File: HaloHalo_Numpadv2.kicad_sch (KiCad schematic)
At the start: 92 parts, among them SW1 SW_SPST, SW10 SW_SPST, SW11 SW_SPST, SW12 SW_SPST, SW13 SW_SPST, SW14 SW_SPST, SW15 SW_SPST, SW16 SW_SPST, SW17 SW_SPST, SW18 SW_SPST, SW19 SW_SPST, SW2 SW_SPST, SW20 SW_SPST, SW21 RotaryEncoder_Switch, SW22 RotaryEncoder_Switch, SW23 RotaryEncoder_Switch, SW3 SW_SPST, SW4 SW_SPST, SW5 SW_SPST, SW6 SW_SPST, SW7 SW_SPST, SW8 SW_SPST, SW9 SW_SPST

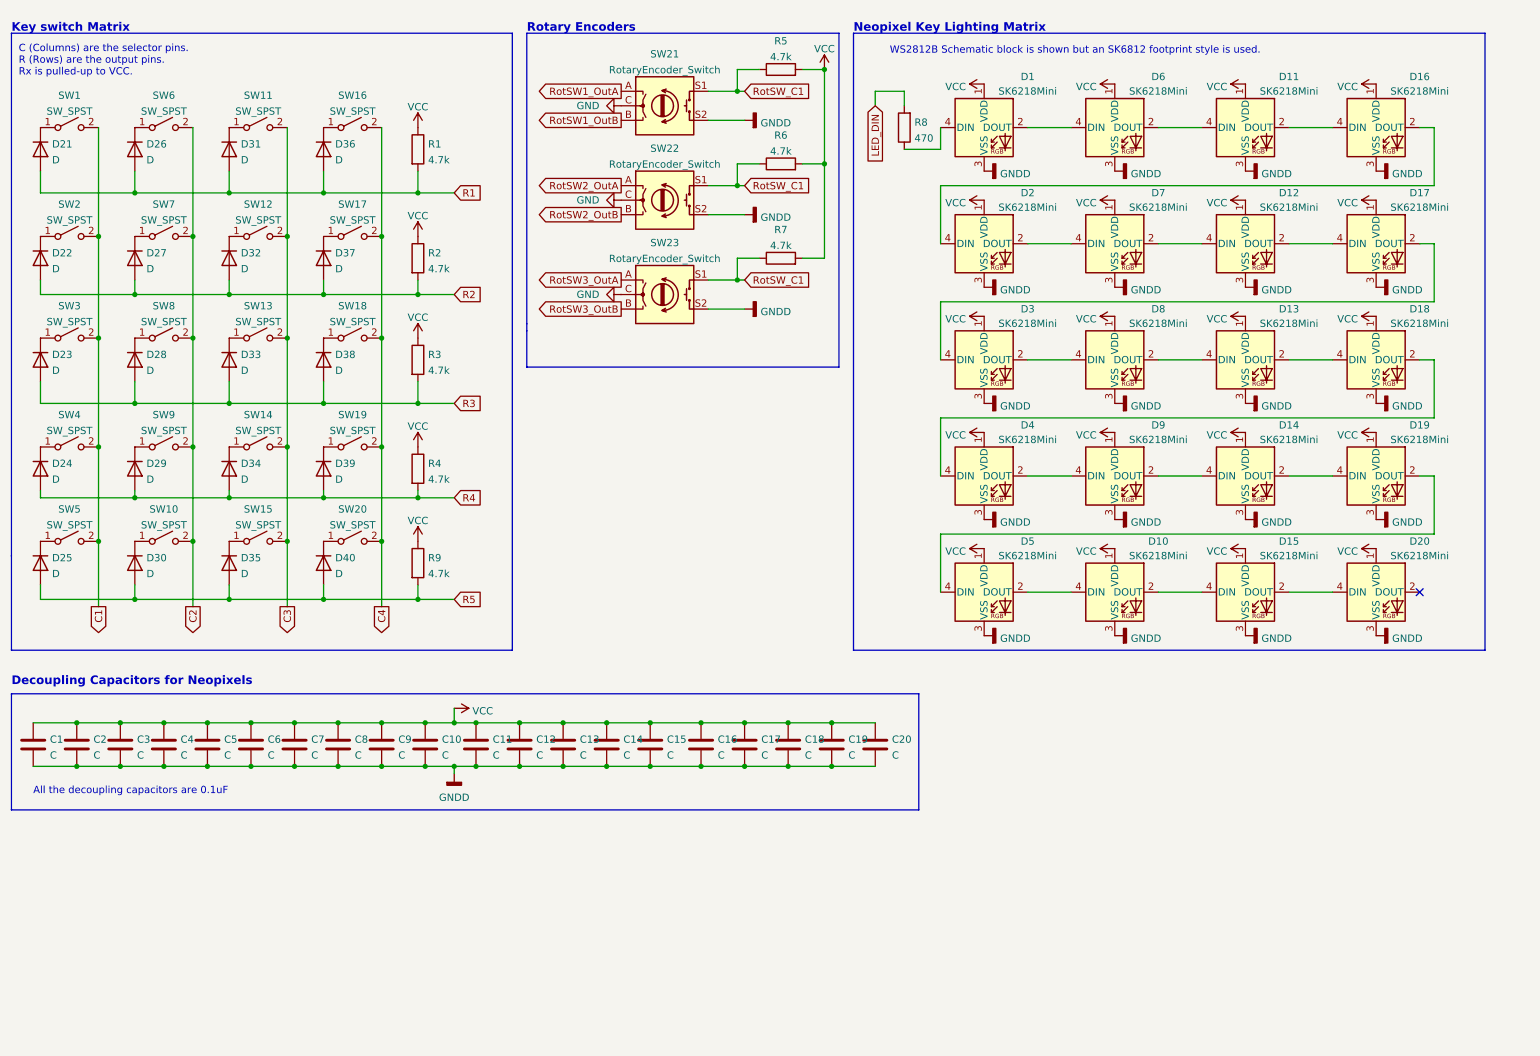
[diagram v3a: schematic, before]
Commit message: Updated Schematic and PCB to include headers for OLED display. Need to update corresponding PDFs and images.
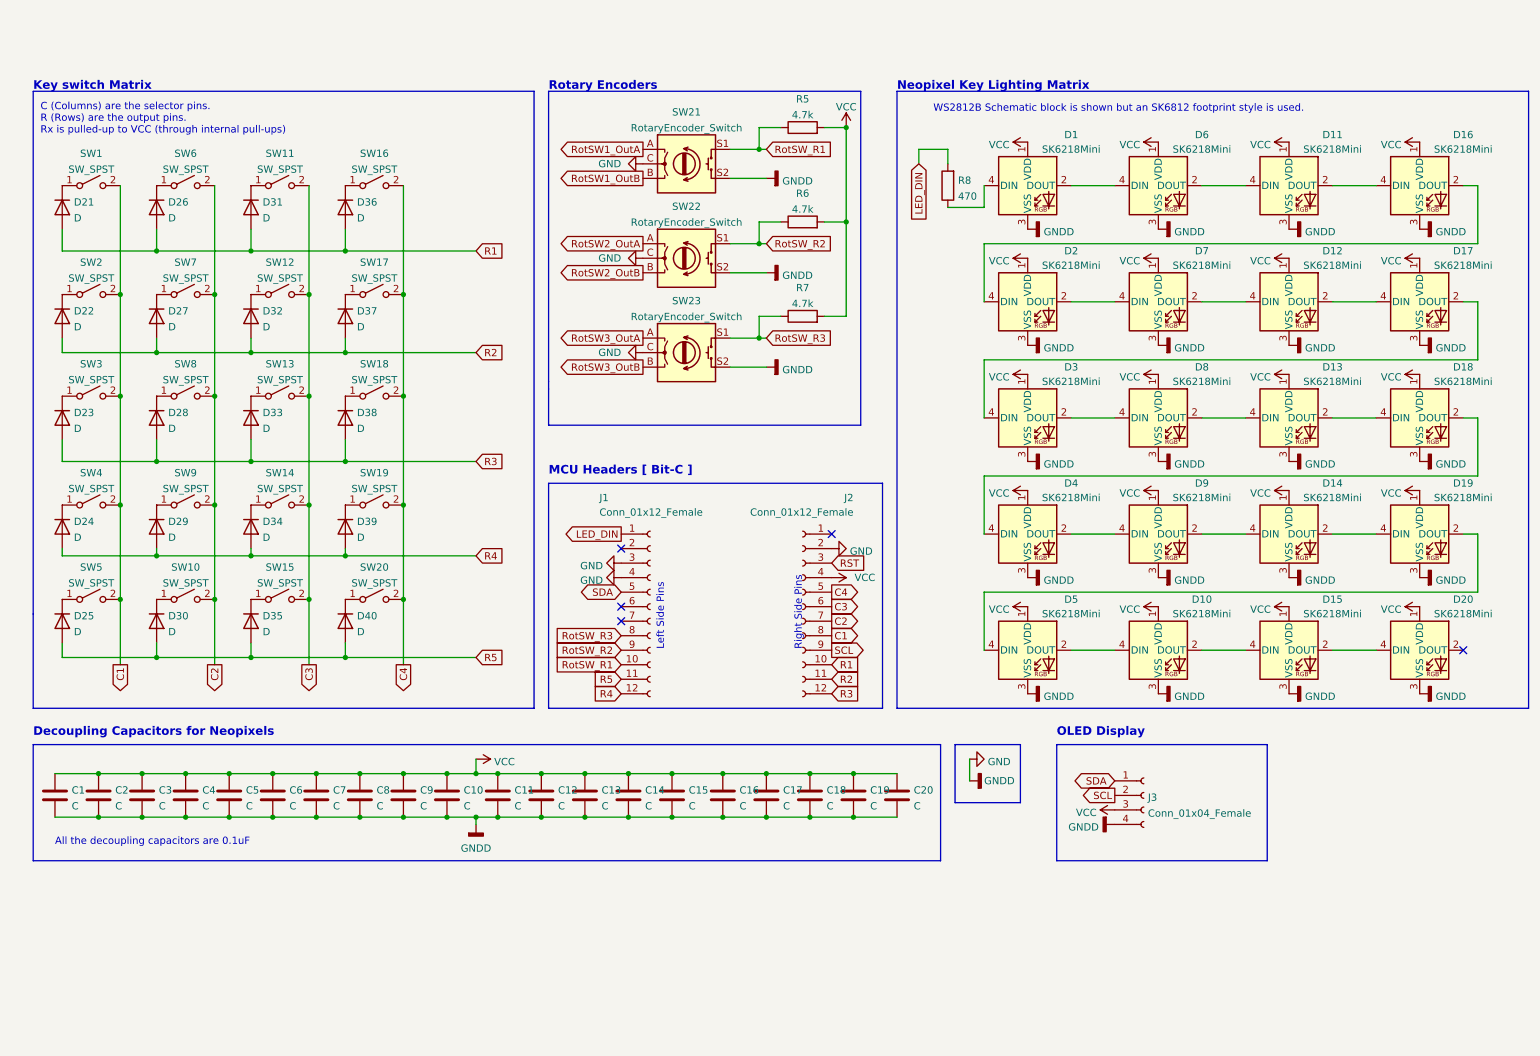
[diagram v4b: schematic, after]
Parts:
- removed R1, R2, R3, R4, R9: 4.7k, Resistor_THT:R_Axial_DIN0204_L3.6mm_D1.6mm_P5.08mm_Horizontal, symbol Device:R
- added J1, J2: Conn_01x12_Female, Connector_PinSocket_2.54mm:PinSocket_1x12_P2.54mm_Vertical, symbol Connector:Conn_01x12_Female
- added J3: Conn_01x04_Female, Connector_PinSocket_2.54mm:PinSocket_1x04_P2.54mm_Vertical, symbol Connector:Conn_01x04_Female
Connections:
- net GNDD is gone; now on net GND: C1.2, C10.2, C11.2, C12.2, C13.2, C14.2, C15.2, C16.2, C17.2, C18.2, C19.2, C2.2, C20.2, C3.2, C4.2, C5.2, C6.2, C7.2, C8.2, C9.2, D1.3 (VSS), D10.3 (VSS), D11.3 (VSS), D12.3 (VSS), D13.3 (VSS), D14.3 (VSS), D15.3 (VSS), D16.3 (VSS), D17.3 (VSS), D18.3 (VSS), D19.3 (VSS), D2.3 (VSS), D20.3 (VSS), D3.3 (VSS), D4.3 (VSS), D5.3 (VSS), D6.3 (VSS), D7.3 (VSS), D8.3 (VSS), D9.3 (VSS), SW21.S2, SW22.S2, SW23.S2
- net C1: now also J2.8 (Pin_8)
- net C2: now also J2.7 (Pin_7)
- net C3: now also J2.6 (Pin_6)
- net C4: now also J2.5 (Pin_5)
- net GND: now also J1.3 (Pin_3), J1.4 (Pin_4), J2.2 (Pin_2), J3.4 (Pin_4)
- net LED_DIN: now also J1.1 (Pin_1)
- net R1: now also J2.10 (Pin_10)
- net R2: now also J2.11 (Pin_11)
- net R3: now also J2.12 (Pin_12)
- net R4: now also J1.12 (Pin_12)
- net R5: now also J1.11 (Pin_11)
- net VCC: now also J2.4 (Pin_4), J3.3 (Pin_3)
- removed net RotSW_C1: R5.1, R6.1, R7.1, SW21.S1, SW22.S1, SW23.S1
- new net RST: J2.3 (Pin_3)
- new net RotSW_R1: J1.10 (Pin_10), R5.1, SW21.S1
- new net RotSW_R2: J1.9 (Pin_9), R6.1, SW22.S1
- new net RotSW_R3: J1.8 (Pin_8), R7.1, SW23.S1
- new net SCL: J2.9 (Pin_9), J3.2 (Pin_2)
- new net SDA: J1.5 (Pin_5), J3.1 (Pin_1)
- no-connect marks 1 -> 5
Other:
- note added: "C (Columns) are the selector pins. R (Rows) are the output pins. Rx is pulled-up to VCC (through internal pull-ups)"
- note added: "Left Side Pins"
- note added: "MCU Headers [ Bit-C ]"
- note added: "OLED Display"
- note added: "Right Side Pins"
- note removed: "C (Columns) are the selector pins. R (Rows) are the output pins. Rx is pulled-up to VCC."
- moved on the sheet: C1, C10, C11, C12, C13, C14, C15, C16, C17, C18, C19, C2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

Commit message: Added OLED display headers
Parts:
- removed R5, R6, R7: 4.7k, Resistor_THT:R_Axial_DIN0204_L3.6mm_D1.6mm_P5.08mm_Horizontal, symbol Device:R
